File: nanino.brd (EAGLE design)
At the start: 68.6 x 53.3 mm, 19 parts, among them IC1 ATMEGA168-20P

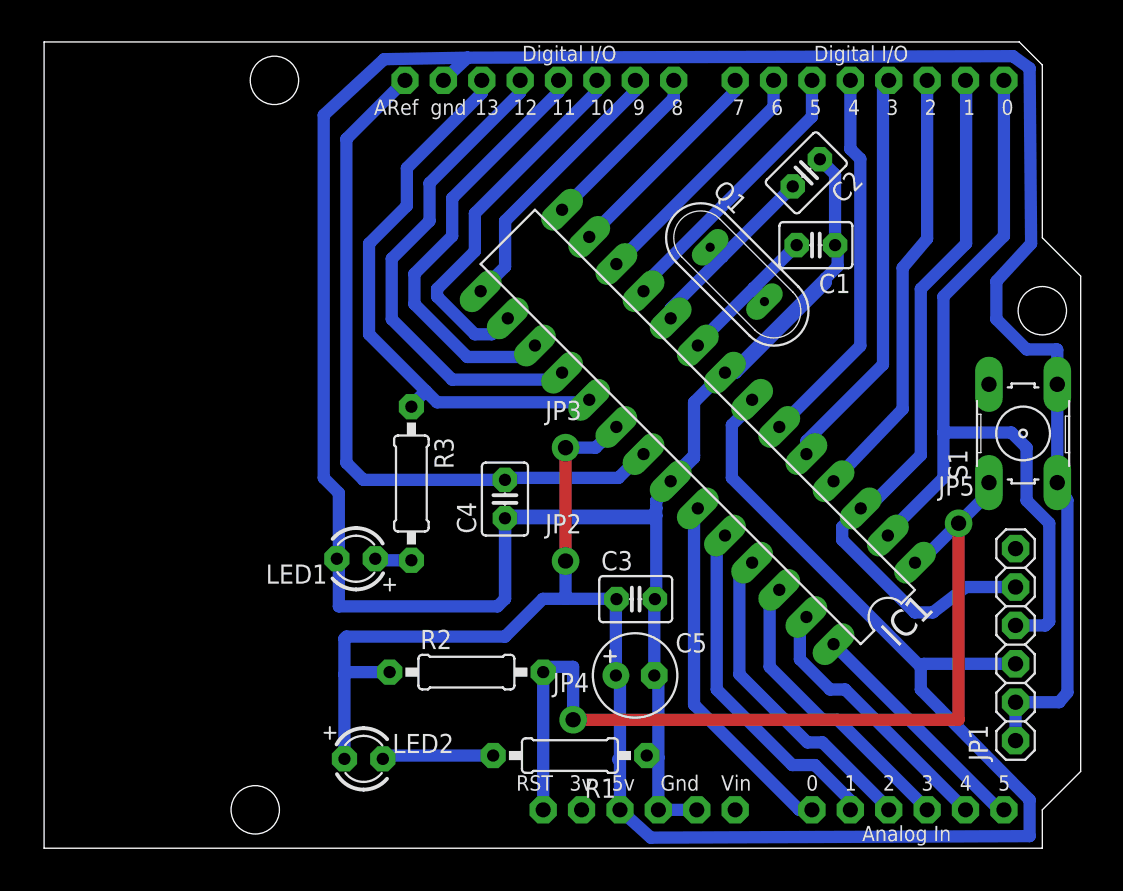
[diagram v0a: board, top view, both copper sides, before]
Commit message: Fablab Imperia fork
Some minor moves, added some clearance, added groundplane, prototyping
zone like the Nanino, some reference values and the text
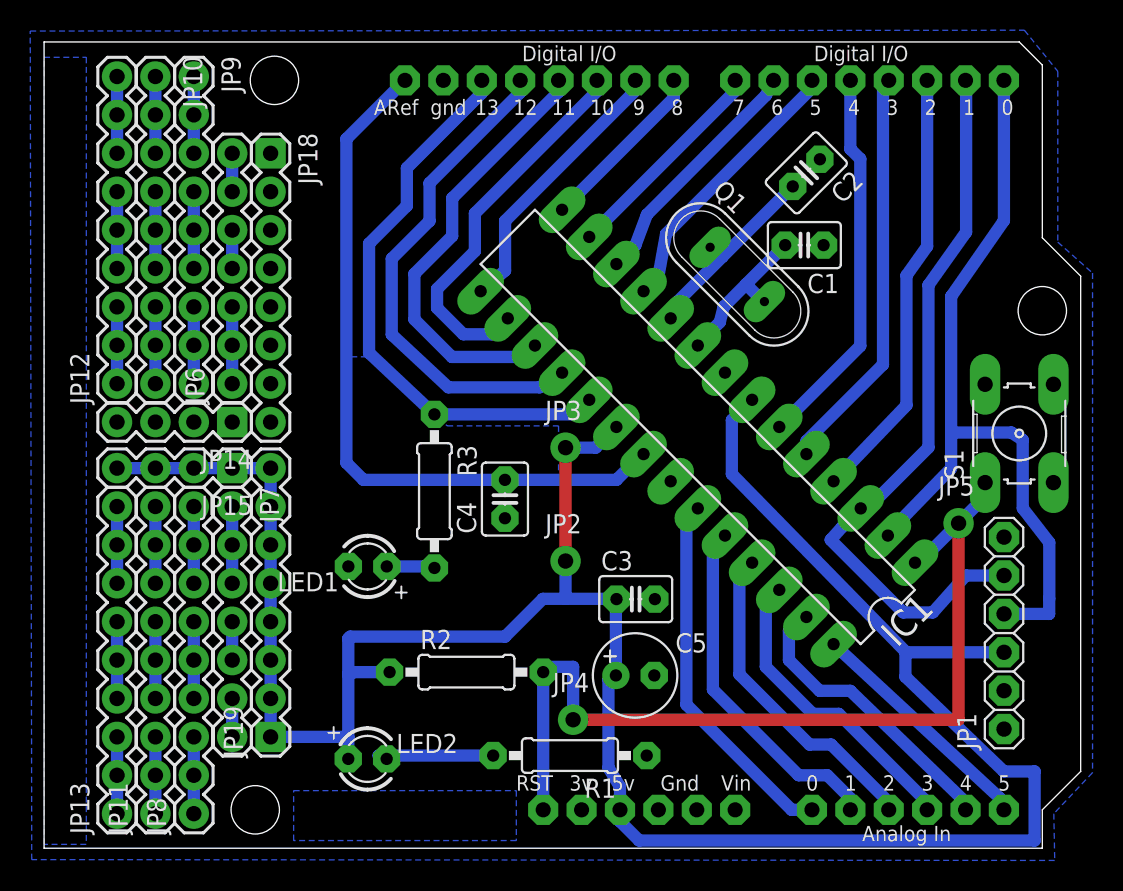
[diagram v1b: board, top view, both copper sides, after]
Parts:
- added JP10, JP11, JP12, JP13, JP8, JP9: M09, SparkFun-Connectors:1X09
- added JP14, JP15: (no value), SparkFun-Connectors:1X04
- added JP18, JP19: (no value), SparkFun-Connectors:1X08
- added JP6, JP7: (no value), SparkFun-Connectors:1X07
- C1, C2: value (none) -> 18-22pF
- C3, C4: value (none) -> 0.1uF
- C5: value (none) -> 1uF
- JP1: value (none) -> GND FTDI DTR
- LED1: value (none) -> pin13
- LED2: value (none) -> power
- Q1: value (none) -> 16MHz
- R1, R3: value (none) -> 1K
- R2: value (none) -> 10K
- S1: value (none) -> reset
- moved R3 1.61 mm to (25.8, 23.6)
- moved JP1 1.08 mm to (63.5, 14.2)
- moved LED1 0.92 mm to (21.4, 18.6)
- moved C1 0.76 mm to (50.3, 39.9)
- moved LED2 0.25 mm to (21.4, 5.91)
- moved S1 0.25 mm to (64.5, 27.4)
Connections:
- net N$11 renamed 3V
- new net N$10: JP11.4, JP11.5, JP11.6
- new net N$11: JP11.7, JP11.8, JP11.9
- new net N$12: JP13.1, JP13.2, JP13.3
- new net N$13: JP13.4, JP13.5, JP13.6
- new net N$14: JP13.7, JP13.8, JP13.9
- new net N$15: JP12.1, JP12.2, JP12.3
- new net N$16: JP12.4, JP12.5, JP12.6
- new net N$17: JP12.7, JP12.8, JP12.9
- new net N$18: JP10.1, JP10.2, JP10.3
- new net N$19: JP10.4, JP10.5, JP10.6
- new net N$20: JP10.7, JP10.8, JP10.9
- new net N$21: JP8.1, JP8.2, JP8.3
- new net N$22: JP8.4, JP8.5, JP8.6
- new net N$23: JP8.7, JP8.8, JP8.9
- new net N$24: JP6.1, JP6.2, JP6.3
- new net N$25: JP6.6, JP6.7
- new net N$26: JP7.1, JP7.2, JP7.3
- new net N$27: JP7.6, JP7.7
- new net N$28: JP6.4, JP6.5
- new net N$29: JP7.4, JP7.5
- new net N$5: JP9.1, JP9.2, JP9.3
- new net N$7: JP9.4, JP9.5, JP9.6
- new net N$8: JP9.7, JP9.8, JP9.9
- new net N$9: JP11.1, JP11.2, JP11.3
- net GND: now also JP14.1, JP14.2, JP14.3, JP14.4, JP18.1, JP18.2, JP18.3, JP18.4, JP18.5, JP18.6, JP18.7, JP18.8
- net VCC: now also JP15.1, JP15.2, JP15.3, JP15.4, JP19.1, JP19.2, JP19.3, JP19.4, JP19.5, JP19.6, JP19.7, JP19.8
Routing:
- net GND: track 243.6 -> 0.00 mm
- net VCC: track 130.4 -> 165.8 mm
- net N$5: track 0.00 -> 5.08 mm
- net N$18: track 0.00 -> 5.08 mm
- net N$17: track 0.00 -> 5.08 mm
- net N$26: track 0.00 -> 5.08 mm
- net N$23: track 0.00 -> 5.08 mm
- net N$14: track 0.00 -> 5.08 mm
- net N$11: track 0.00 -> 5.08 mm
- net N$9: track 0.00 -> 5.08 mm
- net N$22: track 0.00 -> 5.08 mm
- net N$21: track 0.00 -> 5.08 mm
- net N$13: track 0.00 -> 5.08 mm
- net N$12: track 0.00 -> 5.08 mm
- net N$10: track 0.00 -> 5.08 mm
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- added copper zone on layer 16, net GND
- added copper zone on layer 16, net N$6
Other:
- board text added: "NANINO 0.8 (CC-BY-NC-SA)"
- board text added: "Rev. 00"
